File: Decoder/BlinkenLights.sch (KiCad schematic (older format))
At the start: 49 parts, among them Q901 2N7002, Q902 2N7002, Q903 2N7002, Q904 2N7002, Q905 2N7002, U901 74HCT245, U902 74HCT245

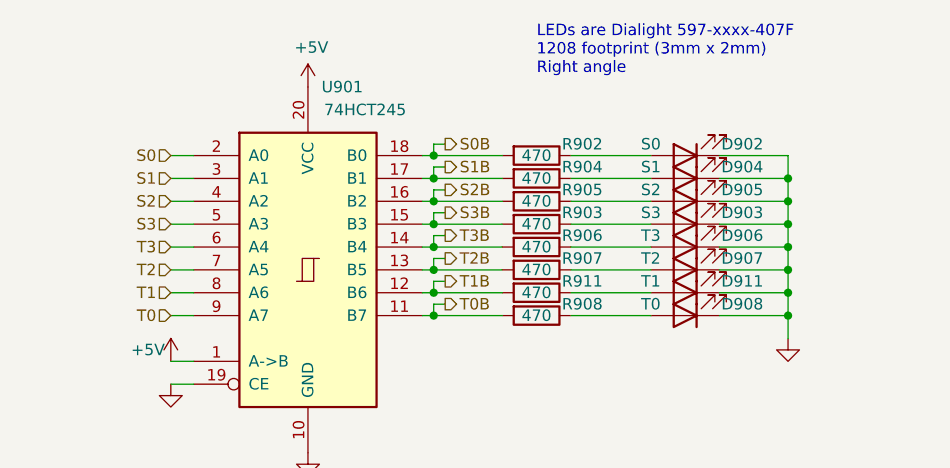
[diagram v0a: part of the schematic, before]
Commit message: Schematics for display & keyboard, adding LEDs to processor PCB
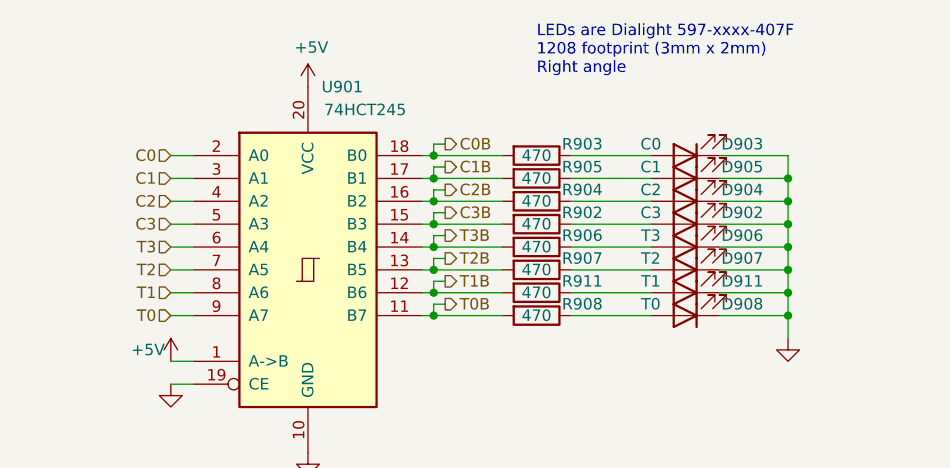
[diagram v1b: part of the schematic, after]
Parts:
- D902: value S0 -> C3
- D903: value S3 -> C0
- D904: value S1 -> C2
- D905: value S2 -> C1
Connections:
- net S0 renamed C0
- net S0B renamed C0B
- net C0B: now also R903.2; no longer R902.2
- net S1 renamed C1
- net S1B renamed C1B
- net C1B: now also R905.2; no longer R904.2
- net S2 renamed C2
- net S2B renamed C2B
- net C2B: now also R904.2; no longer R905.2
- net S3 renamed C3
- net S3B renamed C3B
- net C3B: now also R902.2; no longer R903.2
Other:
- moved on the sheet: D902, D903, D904, D905, R902, R903, R904, R905
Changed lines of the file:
@@
 T3
 Text HLabel 1450 1350 0    50   Input ~ 0
-S0
+C0
 Text HLabel 1450 1450 0    50   Input ~ 0
-S1
+C1
 Text HLabel 1450 1550 0    50   Input ~ 0
-S2
+C2
 Text HLabel 1450 1650 0    50   Input ~ 0
-S3
+C3
 Text HLabel 5850 4800 0    50   Input ~ 0
 INH_MEM
@@
 L Device:R R902
 U 1 1 63A750E9
+P 3050 1650
+F 0 "R902" V 3000 1850 50  0000 C CNN
+F 1 "470" V 3050 1650 50  0000 C CNN
+F 2 "Resistor_SMD:R_0805_2012Metric_Pad1.20x1.40mm_HandSolder" V 2980 1650 50  0001 C CNN
+F 3 "~" H 3050 1650 50  0001 C CNN
+	1    3050 1650
+	0    1    1    0
+$EndComp
+$Comp
+L Device:R R904
+U 1 1 63A75152
+P 3050 1550
+F 0 "R904" V 3000 1750 50  0000 C CNN
+F 1 "470" V 3050 1550 50  0000 C CNN
+F 2 "Resistor_SMD:R_0805_2012Metric_Pad1.20x1.40mm_HandSolder" V 2980 1550 50  0001 C CNN
+F 3 "~" H 3050 1550 50  0001 C CNN
+	1    3050 1550
+	0    1    1    0
+$EndComp
+$Comp
+L Device:R R905
+U 1 1 63A751BB
+P 3050 1450
+F 0 "R905" V 3000 1650 50  0000 C CNN
+F 1 "470" V 3050 1450 50  0000 C CNN
+F 2 "Resistor_SMD:R_0805_2012Metric_Pad1.20x1.40mm_HandSolder" V 2980 1450 50  0001 C CNN
+F 3 "~" H 3050 1450 50  0001 C CNN
+	1    3050 1450
+	0    1    1    0
+$EndComp
+$Comp
+L Device:R R903
+U 1 1 63A75634
 P 3050 1350
-F 0 "R902" V 3000 1550 50  0000 C CNN
+F 0 "R903" V 3000 1550 50  0000 C CNN
 F 1 "470" V 3050 1350 50  0000 C CNN
 F 2 "Resistor_SMD:R_0805_2012Metric_Pad1.20x1.40mm_HandSolder" V 2980 1350 50  0001 C CNN
 F 3 "~" H 3050 1350 50  0001 C CNN
 	1    3050 1350
-	0    1    1    0
-$EndComp
-$Comp
-L Device:R R904
-U 1 1 63A75152
-P 3050 1450
-F 0 "R904" V 3000 1650 50  0000 C CNN
-F 1 "470" V 3050 1450 50  0000 C CNN
-F 2 "Resistor_SMD:R_0805_2012Metric_Pad1.20x1.40mm_HandSolder" V 2980 1450 50  0001 C CNN
-F 3 "~" H 3050 1450 50  0001 C CNN
-	1    3050 1450
-	0    1    1    0
-$EndComp
-$Comp
-L Device:R R905
-U 1 1 63A751BB
-P 3050 1550
-F 0 "R905" V 3000 1750 50  0000 C CNN
-F 1 "470" V 3050 1550 50  0000 C CNN
-F 2 "Resistor_SMD:R_0805_2012Metric_Pad1.20x1.40mm_HandSolder" V 2980 1550 50  0001 C CNN
-F 3 "~" H 3050 1550 50  0001 C CNN
-	1    3050 1550
-	0    1    1    0
-$EndComp
-$Comp
-L Device:R R903
-U 1 1 63A75634
-P 3050 1650
-F 0 "R903" V 3000 1850 50  0000 C CNN
-F 1 "470" V 3050 1650 50  0000 C CNN
-F 2 "Resistor_SMD:R_0805_2012Metric_Pad1.20x1.40mm_HandSolder" V 2980 1650 50  0001 C CNN
-F 3 "~" H 3050 1650 50  0001 C CNN
-	1    3050 1650
 	0    1    1    0
 $EndComp
@@
 L Device:LED D902
 U 1 1 63D1E627
+P 3700 1650
+F 0 "D902" H 3450 1600 50  0000 C CNN
+F 1 "C3" H 3850 1600 50  0000 C CNN
+F 2 "Datapoint2200:LED_Dialight_597_xxxx_407F_SMT_RA_3mmx2mmx1mm" H 3700 1650 50  0001 C CNN
+F 3 "~" H 3700 1650 50  0001 C CNN
+	1    3700 1650
+	-1   0    0    1
+$EndComp
+$Comp
+L Device:LED D904
+U 1 1 63D1E849
+P 3700 1550
+F 0 "D904" H 3450 1500 50  0000 C CNN
+F 1 "C2" H 3850 1500 50  0000 C CNN
+F 2 "Datapoint2200:LED_Dialight_597_xxxx_407F_SMT_RA_3mmx2mmx1mm" H 3700 1550 50  0001 C CNN
+F 3 "~" H 3700 1550 50  0001 C CNN
+	1    3700 1550
+	-1   0    0    1
+$EndComp
+$Comp
+L Device:LED D905
+U 1 1 63D1EA83
+P 3700 1450
+F 0 "D905" H 3450 1400 50  0000 C CNN
+F 1 "C1" H 3850 1400 50  0000 C CNN
+F 2 "Datapoint2200:LED_Dialight_597_xxxx_407F_SMT_RA_3mmx2mmx1mm" H 3700 1450 50  0001 C CNN
+F 3 "~" H 3700 1450 50  0001 C CNN
+	1    3700 1450
+	-1   0    0    1
+$EndComp
+$Comp
+L Device:LED D903
+U 1 1 63D1ECA0
 P 3700 1350
-F 0 "D902" H 3450 1300 50  0000 C CNN
-F 1 "S0" H 3850 1300 50  0000 C CNN
+F 0 "D903" H 3450 1300 50  0000 C CNN
+F 1 "C0" H 3850 1300 50  0000 C CNN
 F 2 "Datapoint2200:LED_Dialight_597_xxxx_407F_SMT_RA_3mmx2mmx1mm" H 3700 1350 50  0001 C CNN
 F 3 "~" H 3700 1350 50  0001 C CNN
 	1    3700 1350
-	-1   0    0    1
-$EndComp
-$Comp
-L Device:LED D904
-U 1 1 63D1E849
-P 3700 1450
-F 0 "D904" H 3450 1400 50  0000 C CNN
-F 1 "S1" H 3850 1400 50  0000 C CNN
-F 2 "Datapoint2200:LED_Dialight_597_xxxx_407F_SMT_RA_3mmx2mmx1mm" H 3700 1450 50  0001 C CNN
-F 3 "~" H 3700 1450 50  0001 C CNN
-	1    3700 1450
-	-1   0    0    1
-$EndComp
-$Comp
-L Device:LED D905
-U 1 1 63D1EA83
-P 3700 1550
-F 0 "D905" H 3450 1500 50  0000 C CNN
-F 1 "S2" H 3850 1500 50  0000 C CNN
-F 2 "Datapoint2200:LED_Dialight_597_xxxx_407F_SMT_RA_3mmx2mmx1mm" H 3700 1550 50  0001 C CNN
-F 3 "~" H 3700 1550 50  0001 C CNN
-	1    3700 1550
-	-1   0    0    1
-$EndComp
-$Comp
-L Device:LED D903
-U 1 1 63D1ECA0
-P 3700 1650
-F 0 "D903" H 3450 1600 50  0000 C CNN
-F 1 "S3" H 3850 1600 50  0000 C CNN
-F 2 "Datapoint2200:LED_Dialight_597_xxxx_407F_SMT_RA_3mmx2mmx1mm" H 3700 1650 50  0001 C CNN
-F 3 "~" H 3700 1650 50  0001 C CNN
-	1    3700 1650
 	-1   0    0    1
 $EndComp
@@
 	2950 3750 3300 3750
 Wire Wire Line
-	3550 1350 3200 1350
-Wire Wire Line
-	3200 1650 3550 1650
-Wire Wire Line
-	3550 1450 3200 1450
-Wire Wire Line
-	3200 1550 3550 1550
+	3550 1650 3200 1650
+Wire Wire Line
+	3200 1350 3550 1350
+Wire Wire Line
+	3550 1550 3200 1550
+Wire Wire Line
+	3200 1450 3550 1450
 Wire Wire Line
 	3550 1750 3200 1750
@@
 $EndComp
 Wire Wire Line
-	3850 1350 4150 1350
-Wire Wire Line
-	4150 1650 3850 1650
-Wire Wire Line
-	3850 1450 4150 1450
-Connection ~ 4150 1550
-Wire Wire Line
-	4150 1550 3850 1550
+	3850 1650 4150 1650
+Wire Wire Line
+	4150 1350 3850 1350
+Wire Wire Line
+	3850 1550 4150 1550
+Wire Wire Line
+	4150 1450 3850 1450
 Wire Wire Line
 	3850 1750 4150 1750
-Connection ~ 4150 1750
 Wire Wire Line
 	4150 1750 4150 1850
@@
 $EndComp
 Text HLabel 2650 1300 2    50   Output ~ 0
-S0B
+C0B
 Text HLabel 2650 1600 2    50   Output ~ 0
-S3B
+C3B
 Text HLabel 2650 1400 2    50   Output ~ 0
-S1B
+C1B
 Text HLabel 2650 1500 2    50   Output ~ 0
-S2B
+C2B
 Text HLabel 2650 1700 2    50   Output ~ 0
 T3B
@@
 	2600 1350 2900 1350
 Wire Wire Line
+	4150 1450 4150 1550
+Wire Wire Line
 	4150 1350 4150 1450
-Connection ~ 4150 1450
-Wire Wire Line
-	4150 1450 4150 1550
-Wire Wire Line
-	4150 1550 4150 1650
-Connection ~ 4150 1650
-Wire Wire Line
-	4150 1650 4150 1750
 Wire Wire Line
 	2550 1450 2600 1450
@@
 Wire Wire Line
 	4150 2050 4150 2150
+Connection ~ 4150 1450
+Wire Wire Line
+	4150 1550 4150 1650
+Connection ~ 4150 1550
+Connection ~ 4150 1750
+Connection ~ 4150 1650
+Wire Wire Line
+	4150 1650 4150 1750
 $EndSCHEMATC
